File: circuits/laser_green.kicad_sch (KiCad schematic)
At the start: 10 parts, among them Q3 AO3400A, U7 TLV9001

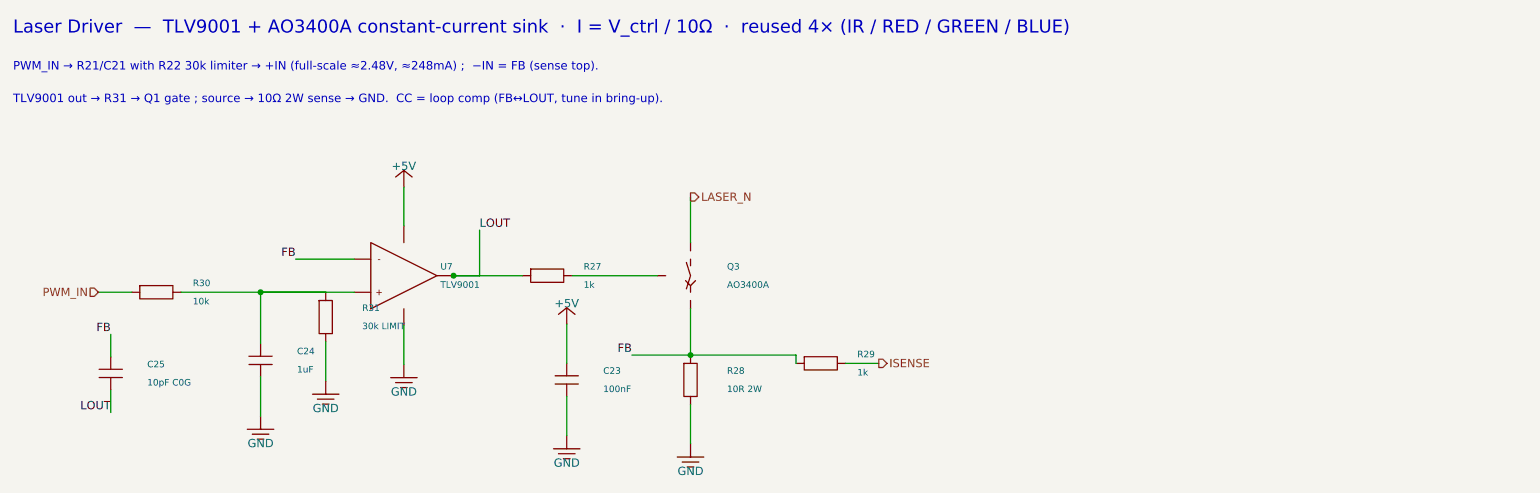
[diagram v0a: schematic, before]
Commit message: chore(circuits): update laser controller release artifacts
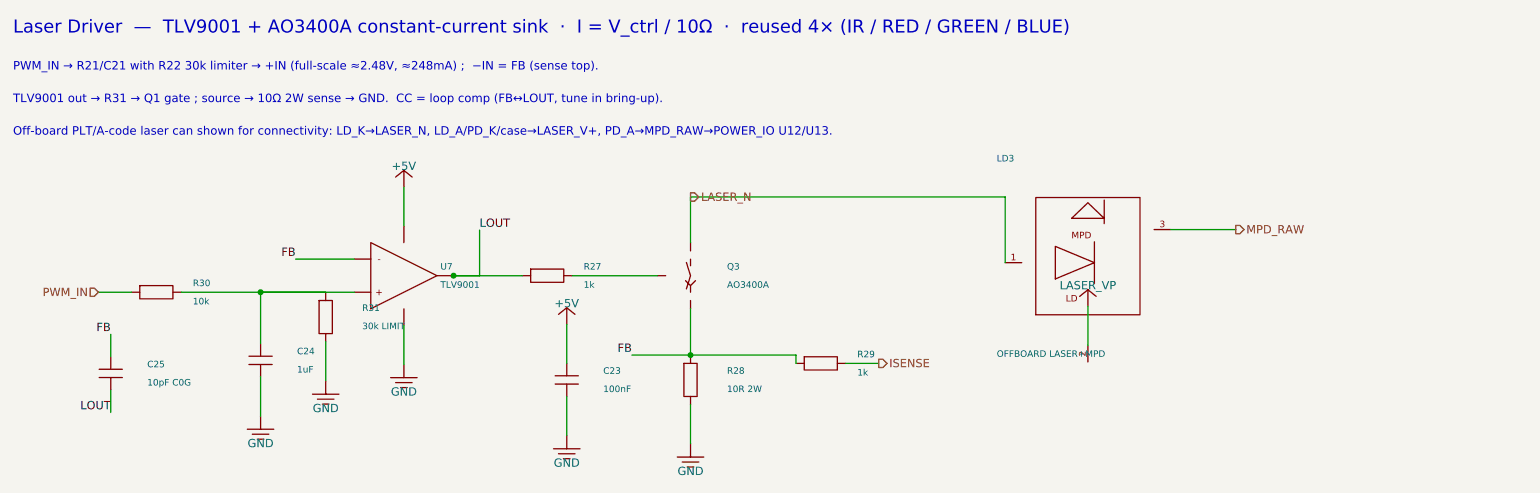
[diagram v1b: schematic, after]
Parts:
- added LD3: OFFBOARD LASER+MPD, symbol viv:LASER_CAN_MON_PD
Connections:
- net LASER_N: now also LD3.1 (LD_K)
- new net LASER_V+: LD3.2 (LD_A/PD_K/CASE)
- new net MPD_RAW: LD3.3 (PD_A)
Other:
- note added: "Off-board PLT/A-code laser can shown for connectivity: LD_K→LASER_N, LD_A/PD_K/case→LASER_V+, PD_A→MPD_RAW→POWER_IO U12/U13."
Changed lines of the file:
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@@
+    )
+  )
+  (symbol (lib_id "viv:LASER_CAN_MON_PD") (at 315 150 0) (unit 1)
+    (in_bom no) (on_board yes) (dnp no)
+    (property "Reference" "LD3" (at 301 134 0) (effects (font (size 1.0 1.0)) (justify left)))
+    (property "Value" "OFFBOARD LASER+MPD" (at 301 164 0) (effects (font (size 1.0 1.0)) (justify left)))
+    (property "Footprint" "" (at 315 150 0) (effects (font (size 1.0 1.0)) hide))
+    (property "Datasheet" "" (at 315 150 0) (effects (font (size 1.0 1.0)) hide))
+    (property "Part Number" "" (at 315 150 0) (effects (font (size 1.0 1.0)) hide))
+    (property "LCSC" "" (at 315 150 0) (effects (font (size 1.0 1.0)) hide))
+    (pin "1")
+    (pin "2")
+    (pin "3")
+    (instances
+      (project "laser_controller"
+        (path "/c1d2e3f4-6000-4000-a000-000000000001" (reference "LD3") (unit 1))
+      )
     )
   )
@@
       (project "laser_controller"
         (path "/c1d2e3f4-6000-4000-a000-000000000001" (reference "#PWR07") (unit 1))
+      )
+    )
+  )
+  (symbol (lib_id "viv:LASER_VP") (at 315 156.7 0) (unit 1)
+    (in_bom no) (on_board yes) (dnp no)
+    (property "Reference" "#PWR08" (at 315 153.7 0) (effects (font (size 1.0 1.0)) hide))
+    (property "Value" "LASER_VP" (at 315 153.5 0) (effects (font (size 1.27 1.27))))
+    (property "Footprint" "" (at 0 0 0) (effects (font (size 1.0 1.0)) hide))
+    (property "Datasheet" "" (at 0 0 0) (effects (font (size 1.0 1.0)) hide))
+    (pin "1")
+    (instances
+      (project "laser_controller"
+        (path "/c1d2e3f4-6000-4000-a000-000000000001" (reference "#PWR08") (unit 1))
       )
     )
@@
   (wire (pts (xy 277.81 165.46) (xy 282.89 165.46)) (stroke (width 0) (type default)))
   (wire (pts (xy 254 146.92) (xy 254 139.92)) (stroke (width 0) (type default)))
+  (wire (pts (xy 254 139.92) (xy 302.3 139.92)) (stroke (width 0) (type default)))
+  (wire (pts (xy 302.3 139.92) (xy 302.3 150)) (stroke (width 0) (type default)))
+  (wire (pts (xy 315 162.7) (xy 315 156.7)) (stroke (width 0) (type default)))
+  (wire (pts (xy 327.7 144.92) (xy 337.7 144.92)) (stroke (width 0) (type default)))
   (wire (pts (xy 202.38 149.46) (xy 193.38 149.46)) (stroke (width 0) (type default)))
   (wire (pts (xy 254 164.19) (xy 245 164.19)) (stroke (width 0) (type default)))
@@
   (hierarchical_label "ISENSE" (shape output) (at 282.89 165.46 0) (effects (font (size 1.27 1.27)) (justify left)))
   (hierarchical_label "LASER_N" (shape output) (at 254 139.92 0) (effects (font (size 1.27 1.27)) (justify left)))
+  (hierarchical_label "MPD_RAW" (shape output) (at 337.7 144.92 0) (effects (font (size 1.27 1.27)) (justify left)))
   (label "FB" (at 193.38 149.46 0) (effects (font (size 1.27 1.27)) (justify right bottom)))
   (label "FB" (at 245 164.19 0) (effects (font (size 1.27 1.27)) (justify right bottom)))
@@
   (text "PWM_IN → R21/C21 with R22 30k limiter → +IN (full-scale ≈2.48V, ≈248mA) ;  −IN = FB (sense top)." (at 150 120 0) (effects (font (size 1.3 1.3)) (justify left)))
   (text "TLV9001 out → R31 → Q1 gate ; source → 10Ω 2W sense → GND.  CC = loop comp (FB↔LOUT, tune in bring-up)." (at 150 125 0) (effects (font (size 1.3 1.3)) (justify left)))
+  (text "Off-board PLT/A-code laser can shown for connectivity: LD_K→LASER_N, LD_A/PD_K/case→LASER_V+, PD_A→MPD_RAW→POWER_IO U12/U13." (at 150 130 0) (effects (font (size 1.3 1.3)) (justify left)))
   (sheet_instances
     (path "/" (page "1"))

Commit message: fix(circuits): import mcu sheet and laser footprints
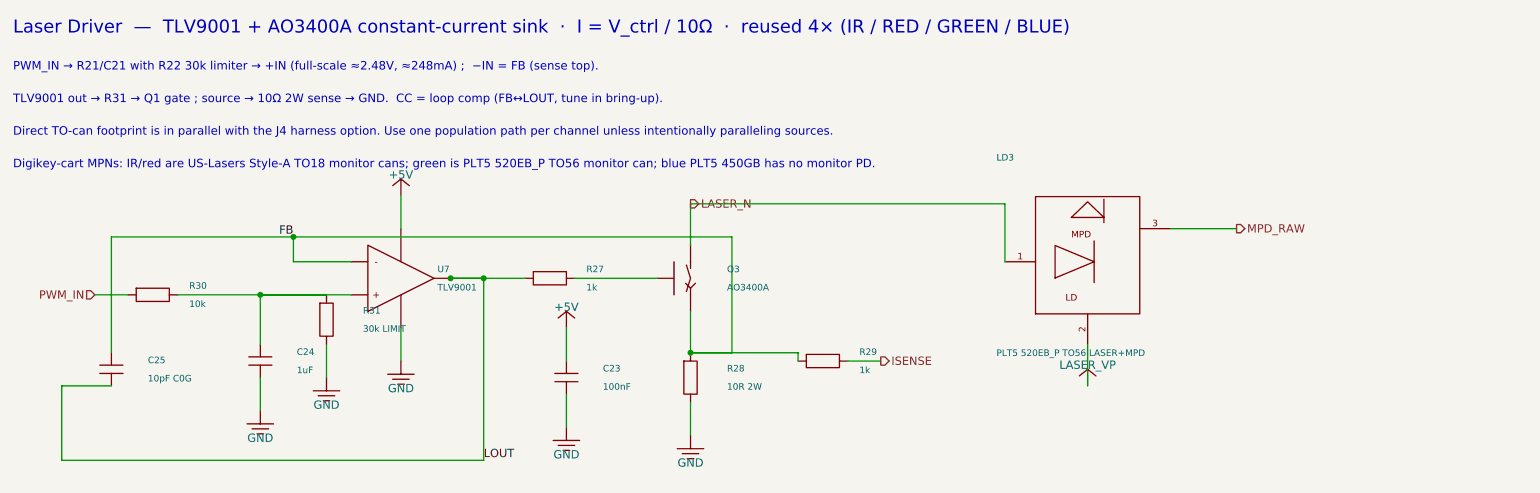
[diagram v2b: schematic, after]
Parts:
- removed LD3: OFFBOARD LASER+MPD, symbol viv:LASER_CAN_MON_PD
- removed Q3: AO3400A, Package_TO_SOT_SMD:SOT-23, symbol viv:NMOS
- added R28: 10R 2W, Resistor_SMD:R_2512_6332Metric_Pad1.40x3.35mm_HandSolder, symbol viv:R_V
- added R30: 10k, Resistor_SMD:R_0603_1608Metric_Pad0.98x0.95mm_HandSolder, symbol viv:R_H
- C23: LCSC C1525 -> C83056; Part Number CL05B104KO5NNNC -> 0402B104K160CT
- C24: LCSC C52923 -> C7472946; Part Number CL05A105KA5NQNC -> HGC0402R5105K250NTEJ
- LD3: renamed from R30; value 10k -> PLT5 520EB_P TO56 LASER+MPD; footprint Resistor_SMD:R_0603_1608Metric_Pad0.98x0.95mm_HandSolder -> OptoDevice:LaserDiode_TO56-3; symbol viv:R_H -> viv:LASER_CAN_MON_PD; LCSC C269701 -> (none); Part Number 0603WAF1002T5E -> PLT5 520EB_P; now left out of the parts list
- Q3: renamed from R28; value 10R 2W -> AO3400A; footprint Resistor_SMD:R_2512_6332Metric_Pad1.40x3.35mm_HandSolder -> Package_TO_SOT_SMD:SOT-23; symbol viv:R_V -> viv:NMOS; LCSC C5123624 -> C20917; Part Number HoCR2512-2W-10R-1% -> AO3400A
- R27, R29: LCSC C21190 -> C2907002; Part Number 0603WAF1001T5E -> FRC0603F1001TS
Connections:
- net FB: now also Q3.2 (S), R28.1; no longer Q3.1
- net GND: now also R28.2; no longer Q3.2
- net LASER_N: now also LD3.1 (LD_K), Q3.3 (D)
- net LASER_V+: now also LD3.2 (LD_A/PD_K/CASE)
- net MPD_RAW: now also LD3.3 (PD_A)
- net PWM_IN: now also R30.1; no longer LD3.1
- net at C24.1, R31.1, U7.3 (+): now also R30.2; no longer LD3.2
- net at R27.2: now also Q3.1 (G)
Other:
- note added: "Digikey-cart MPNs: IR/red are US-Lasers Style-A TO18 monitor cans; green is PLT5 520EB_P TO56 monitor can; blue PLT5 450GB has no monitor PD."
- note added: "Direct TO-can footprint is in parallel with the J4 harness option. Use one population path per channel unless intentionally paralleling sources."
- note removed: "Off-board PLT/A-code laser can shown for connectivity: LD_K→LASER_N, LD_A/PD_K/case→LASER_V+, PD_A→MPD_RAW→POWER_IO U12/U13."

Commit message: save laser controller schematic and layout state
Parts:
- removed R30: 10k, Resistor_SMD:R_0603_1608Metric_Pad0.98x0.95mm_HandSolder, symbol viv:R_H
- removed R31: 30k LIMIT, Resistor_SMD:R_0603_1608Metric_Pad0.98x0.95mm_HandSolder, symbol viv:R_V
- added Q3: AO3400A, Package_TO_SOT_SMD:SOT-23, symbol viv:NMOS
- added R27: 1k, Resistor_SMD:R_0603_1608Metric_Pad0.98x0.95mm_HandSolder, symbol viv:R_H
- R30: renamed from R27; value 1k -> 10k; LCSC C2907002 -> C844918; Part Number FRC0603F1001TS -> CRCW060310K0FKEA
- R31: renamed from Q3; value AO3400A -> 30k LIMIT; footprint Package_TO_SOT_SMD:SOT-23 -> Resistor_SMD:R_0603_1608Metric_Pad0.98x0.95mm_HandSolder; symbol viv:NMOS -> viv:R_V; LCSC C20917 -> C22984; Part Number AO3400A -> 0603WAF3002T5E
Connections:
- net FB: now also Q3.2 (S); no longer R31.2 (S)
- net GND: now also R31.2
- net LASER_N: now also Q3.3 (D); no longer R31.3 (D)
- net LOUT: now also R27.1; no longer R30.1
- net PWM_IN: now also R30.1
- net at C24.1, U7.3 (+): now also R30.2, R31.1
- new net: Q3.1 (G), R27.2
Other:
- moved on the sheet: R30

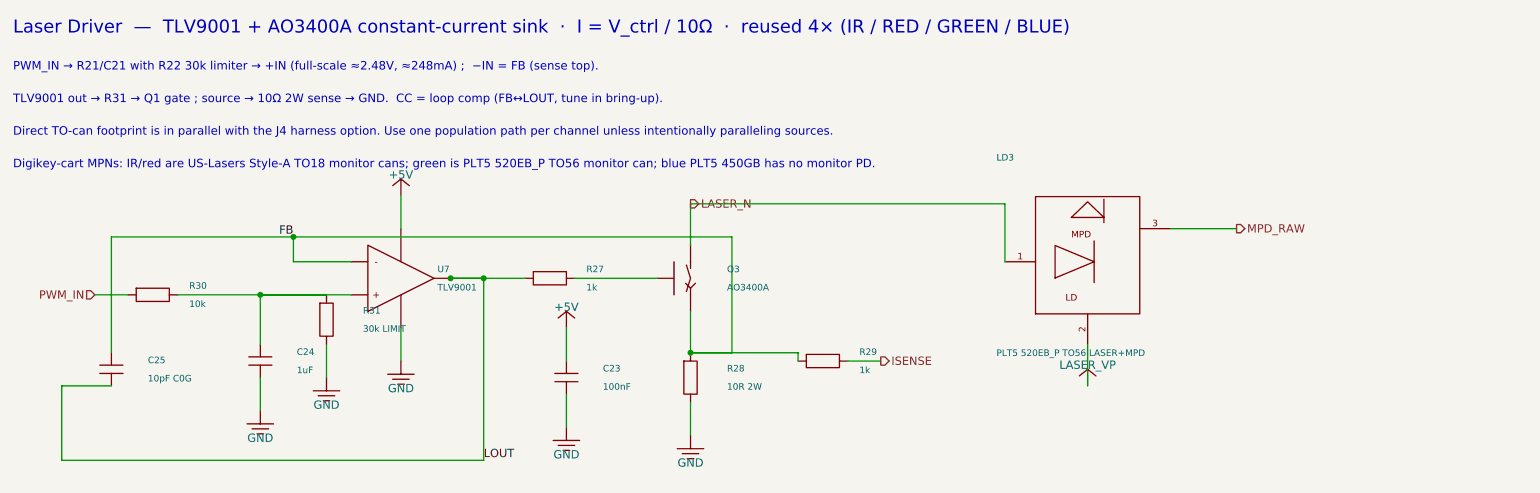
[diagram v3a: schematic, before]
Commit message: save current laser controller recovery state
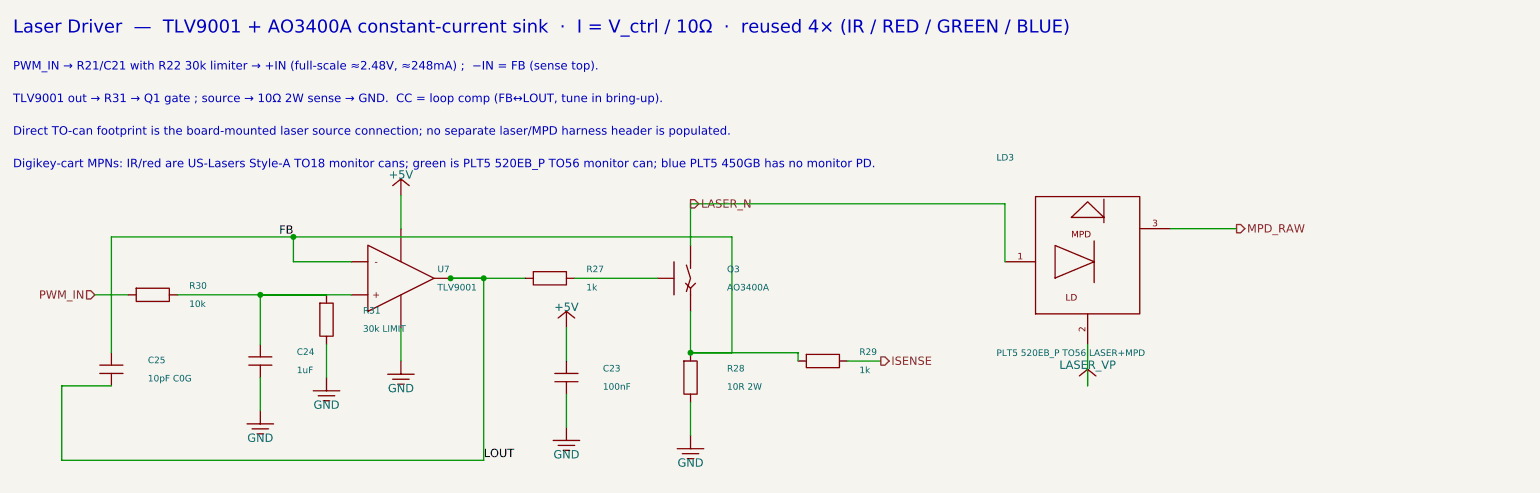
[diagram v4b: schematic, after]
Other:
- note added: "Direct TO-can footprint is the board-mounted laser source connection; no separate laser/MPD harness header is populated."
- note removed: "Direct TO-can footprint is in parallel with the J4 harness option. Use one population path per channel unless intentionally paralleling sources."
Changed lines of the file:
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@@
   (text "PWM_IN → R21/C21 with R22 30k limiter → +IN (full-scale ≈2.48V, ≈248mA) ;  −IN = FB (sense top)." (at 150 120 0) (effects (font (size 1.3 1.3)) (justify left)))
   (text "TLV9001 out → R31 → Q1 gate ; source → 10Ω 2W sense → GND.  CC = loop comp (FB↔LOUT, tune in bring-up)." (at 150 125 0) (effects (font (size 1.3 1.3)) (justify left)))
-  (text "Direct TO-can footprint is in parallel with the J4 harness option. Use one population path per channel unless intentionally paralleling sources." (at 150 130 0) (effects (font (size 1.3 1.3)) (justify left)))
+  (text "Direct TO-can footprint is the board-mounted laser source connection; no separate laser/MPD harness header is populated." (at 150 130 0) (effects (font (size 1.3 1.3)) (justify left)))
   (text "Digikey-cart MPNs: IR/red are US-Lasers Style-A TO18 monitor cans; green is PLT5 520EB_P TO56 monitor can; blue PLT5 450GB has no monitor PD." (at 150 135 0) (effects (font (size 1.3 1.3)) (justify left)))
   (sheet_instances
